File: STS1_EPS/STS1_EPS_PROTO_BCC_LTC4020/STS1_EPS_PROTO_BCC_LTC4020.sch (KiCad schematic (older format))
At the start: 13 parts, among them J1 1729267, J9 Output

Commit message: Reworked BCC
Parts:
- added C10, C9: 56µ, Capacitor_SMD:C_Elec_6.3x5.4, symbol Device:CP
- C1: value C -> 100n; footprint Capacitor_SMD:C_0805_2012Metric -> Capacitor_SMD:C_1812_4532Metric
- C2: value C -> 4µ7; footprint Capacitor_SMD:C_0805_2012Metric -> Capacitor_SMD:C_1812_4532Metric
- C3: value CP -> 56µ; footprint Capacitor_SMD:C_0805_2012Metric -> Capacitor_SMD:C_Elec_6.3x5.4
- renumbered J9 to J2
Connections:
- net EPS Battery Charger/Vout: now also C10.1, C9.1
- net GND: now also C10.2, C9.2
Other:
- moved on the sheet: C1, C2
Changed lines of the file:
@@
 L power:GND #PWR011
 U 1 1 60D46E13
-P 7700 1750
-F 0 "#PWR011" H 7700 1500 50  0001 C CNN
-F 1 "GND" H 7705 1577 50  0000 C CNN
-F 2 "" H 7700 1750 50  0001 C CNN
-F 3 "" H 7700 1750 50  0001 C CNN
-	1    7700 1750
+P 7700 1800
+F 0 "#PWR011" H 7700 1550 50  0001 C CNN
+F 1 "GND" H 7705 1627 50  0000 C CNN
+F 2 "" H 7700 1800 50  0001 C CNN
+F 3 "" H 7700 1800 50  0001 C CNN
+	1    7700 1800
 	1    0    0    -1
 $EndComp
@@
 L power:GND #PWR010
 U 1 1 60D46A71
-P 7350 1750
-F 0 "#PWR010" H 7350 1500 50  0001 C CNN
-F 1 "GND" H 7355 1577 50  0000 C CNN
-F 2 "" H 7350 1750 50  0001 C CNN
-F 3 "" H 7350 1750 50  0001 C CNN
-	1    7350 1750
+P 7300 1800
+F 0 "#PWR010" H 7300 1550 50  0001 C CNN
+F 1 "GND" H 7305 1627 50  0000 C CNN
+F 2 "" H 7300 1800 50  0001 C CNN
+F 3 "" H 7300 1800 50  0001 C CNN
+	1    7300 1800
 	1    0    0    -1
 $EndComp
@@
 L power:GND #PWR09
 U 1 1 60D462E6
-P 7000 1750
-F 0 "#PWR09" H 7000 1500 50  0001 C CNN
-F 1 "GND" H 7005 1577 50  0000 C CNN
-F 2 "" H 7000 1750 50  0001 C CNN
-F 3 "" H 7000 1750 50  0001 C CNN
-	1    7000 1750
+P 6850 1800
+F 0 "#PWR09" H 6850 1550 50  0001 C CNN
+F 1 "GND" H 6855 1627 50  0000 C CNN
+F 2 "" H 6850 1800 50  0001 C CNN
+F 3 "" H 6850 1800 50  0001 C CNN
+	1    6850 1800
 	1    0    0    -1
 $EndComp
@@
 P 7700 1600
 F 0 "C3" H 7818 1646 50  0000 L CNN
-F 1 "CP" H 7818 1555 50  0000 L CNN
-F 2 "Capacitor_SMD:C_0805_2012Metric" H 7738 1450 50  0001 C CNN
-F 3 "~" H 7700 1600 50  0001 C CNN
+F 1 "56µ" H 7818 1555 50  0000 L CNN
+F 2 "Capacitor_SMD:C_Elec_6.3x5.4" H 7738 1450 50  0001 C CNN
+F 3 "https://www.mouser.at/datasheet/2/293/e_gyc-1903391.pdf" H 7700 1600 50  0001 C CNN
 	1    7700 1600
 	1    0    0    -1
 $EndComp
-Wire Wire Line
-	7350 1450 7700 1450
 $Comp
 L Device:C C2
 U 1 1 60D44B49
-P 7350 1600
-F 0 "C2" H 7465 1646 50  0000 L CNN
-F 1 "C" H 7465 1555 50  0000 L CNN
-F 2 "Capacitor_SMD:C_0805_2012Metric" H 7388 1450 50  0001 C CNN
-F 3 "~" H 7350 1600 50  0001 C CNN
-	1    7350 1600
-	1    0    0    -1
-$EndComp
-Connection ~ 7350 1450
-Wire Wire Line
-	7000 1450 7350 1450
+P 7300 1600
+F 0 "C2" H 7415 1646 50  0000 L CNN
+F 1 "4µ7" H 7415 1555 50  0000 L CNN
+F 2 "Capacitor_SMD:C_1812_4532Metric" H 7338 1450 50  0001 C CNN
+F 3 "~" H 7300 1600 50  0001 C CNN
+	1    7300 1600
+	1    0    0    -1
+$EndComp
 $Comp
 L Device:C C1
 U 1 1 60D43AF5
-P 7000 1600
-F 0 "C1" H 7115 1646 50  0000 L CNN
-F 1 "C" H 7115 1555 50  0000 L CNN
-F 2 "Capacitor_SMD:C_0805_2012Metric" H 7038 1450 50  0001 C CNN
-F 3 "~" H 7000 1600 50  0001 C CNN
-	1    7000 1600
-	1    0    0    -1
-$EndComp
-Connection ~ 7000 1450
-Wire Wire Line
-	6000 1450 7000 1450
+P 6850 1600
+F 0 "C1" H 6965 1646 50  0000 L CNN
+F 1 "100n" H 6965 1555 50  0000 L CNN
+F 2 "Capacitor_SMD:C_1812_4532Metric" H 6888 1450 50  0001 C CNN
+F 3 "~" H 6850 1600 50  0001 C CNN
+	1    6850 1600
+	1    0    0    -1
+$EndComp
+Connection ~ 6850 1450
+Wire Wire Line
+	6000 1450 6850 1450
 $Sheet
 S 5300 1350 700  200
@@
 $EndSheet
 $Comp
-L 2021-06-25_11-05-00:1725656 J9
+L 2021-06-25_11-05-00:1725656 J2
 U 1 1 60D71756
 P 10050 1450
-F 0 "J9" H 10578 1453 60  0000 L CNN
+F 0 "J2" H 10578 1453 60  0000 L CNN
 F 1 "Output" H 10578 1347 60  0000 L CNN
 F 2 "footprints:1725656" H 10450 1390 60  0001 C CNN
@@
 $EndComp
 Wire Wire Line
-	10050 1450 7700 1450
+	10050 1450 8600 1450
 Connection ~ 7700 1450
 $Comp
@@
 $EndComp
 $Comp
-L power:GND #PWR0101
+L power:GND #PWR01
 U 1 1 60D850C0
 P 1500 1550
-F 0 "#PWR0101" H 1500 1300 50  0001 C CNN
+F 0 "#PWR01" H 1500 1300 50  0001 C CNN
 F 1 "GND" H 1505 1377 50  0000 C CNN
 F 2 "" H 1500 1550 50  0001 C CNN
@@
 $EndComp
 $Comp
-L power:GND #PWR0102
+L power:GND #PWR02
 U 1 1 60D860B9
 P 1500 1750
-F 0 "#PWR0102" H 1500 1500 50  0001 C CNN
+F 0 "#PWR02" H 1500 1500 50  0001 C CNN
 F 1 "GND" H 1505 1577 50  0000 C CNN
 F 2 "" H 1500 1750 50  0001 C CNN
@@
 $EndComp
 $Comp
-L power:GND #PWR0103
+L power:GND #PWR03
 U 1 1 60D865CE
 P 1500 1950
-F 0 "#PWR0103" H 1500 1700 50  0001 C CNN
+F 0 "#PWR03" H 1500 1700 50  0001 C CNN
 F 1 "GND" H 1505 1777 50  0000 C CNN
 F 2 "" H 1500 1950 50  0001 C CNN
@@
 $EndComp
 $Comp
-L power:GND #PWR0104
+L power:GND #PWR04
 U 1 1 60D8699D
 P 1500 2150
-F 0 "#PWR0104" H 1500 1900 50  0001 C CNN
+F 0 "#PWR04" H 1500 1900 50  0001 C CNN
 F 1 "GND" H 1505 1977 50  0000 C CNN
 F 2 "" H 1500 2150 50  0001 C CNN
@@
 $EndComp
 $Comp
-L power:GND #PWR0105
+L power:GND #PWR05
 U 1 1 60D86C57
 P 1500 2350
-F 0 "#PWR0105" H 1500 2100 50  0001 C CNN
+F 0 "#PWR05" H 1500 2100 50  0001 C CNN
 F 1 "GND" H 1505 2177 50  0000 C CNN
 F 2 "" H 1500 2350 50  0001 C CNN
@@
 $EndComp
 $Comp
-L power:GND #PWR0106
+L power:GND #PWR06
 U 1 1 60D86EA0
 P 1500 2550
-F 0 "#PWR0106" H 1500 2300 50  0001 C CNN
+F 0 "#PWR06" H 1500 2300 50  0001 C CNN
 F 1 "GND" H 1505 2377 50  0000 C CNN
 F 2 "" H 1500 2550 50  0001 C CNN
@@
 $EndComp
 $Comp
-L power:GND #PWR0107
+L power:GND #PWR07
 U 1 1 60D8714D
 P 1500 2750
-F 0 "#PWR0107" H 1500 2500 50  0001 C CNN
+F 0 "#PWR07" H 1500 2500 50  0001 C CNN
 F 1 "GND" H 1505 2577 50  0000 C CNN
 F 2 "" H 1500 2750 50  0001 C CNN
@@
 $EndComp
 $Comp
-L power:GND #PWR0108
+L power:GND #PWR08
 U 1 1 60D874BB
 P 1500 2950
-F 0 "#PWR0108" H 1500 2700 50  0001 C CNN
+F 0 "#PWR08" H 1500 2700 50  0001 C CNN
 F 1 "GND" H 1505 2777 50  0000 C CNN
 F 2 "" H 1500 2950 50  0001 C CNN
@@
 Wire Wire Line
 	2650 2650 2650 2850
+$Comp
+L Device:CP C9
+U 1 1 60DCCB93
+P 8150 1600
+F 0 "C9" H 8268 1646 50  0000 L CNN
+F 1 "56µ" H 8268 1555 50  0000 L CNN
+F 2 "Capacitor_SMD:C_Elec_6.3x5.4" H 8188 1450 50  0001 C CNN
+F 3 "https://www.mouser.at/datasheet/2/293/e_gyc-1903391.pdf" H 8150 1600 50  0001 C CNN
+	1    8150 1600
+	1    0    0    -1
+$EndComp
+$Comp
+L Device:CP C10
+U 1 1 60DCD030
+P 8600 1600
+F 0 "C10" H 8718 1646 50  0000 L CNN
+F 1 "56µ" H 8718 1555 50  0000 L CNN
+F 2 "Capacitor_SMD:C_Elec_6.3x5.4" H 8638 1450 50  0001 C CNN
+F 3 "https://www.mouser.at/datasheet/2/293/e_gyc-1903391.pdf" H 8600 1600 50  0001 C CNN
+	1    8600 1600
+	1    0    0    -1
+$EndComp
+Wire Wire Line
+	6850 1750 6850 1800
+Wire Wire Line
+	7300 1750 7300 1800
+Wire Wire Line
+	7700 1750 7700 1800
+$Comp
+L power:GND #PWR022
+U 1 1 60DCEDB8
+P 8150 1800
+F 0 "#PWR022" H 8150 1550 50  0001 C CNN
+F 1 "GND" H 8155 1627 50  0000 C CNN
+F 2 "" H 8150 1800 50  0001 C CNN
+F 3 "" H 8150 1800 50  0001 C CNN
+	1    8150 1800
+	1    0    0    -1
+$EndComp
+$Comp
+L power:GND #PWR023
+U 1 1 60DCF044
+P 8600 1800
+F 0 "#PWR023" H 8600 1550 50  0001 C CNN
+F 1 "GND" H 8605 1627 50  0000 C CNN
+F 2 "" H 8600 1800 50  0001 C CNN
+F 3 "" H 8600 1800 50  0001 C CNN
+	1    8600 1800
+	1    0    0    -1
+$EndComp
+Wire Wire Line
+	8150 1750 8150 1800
+Wire Wire Line
+	8600 1750 8600 1800
+Connection ~ 8150 1450
+Wire Wire Line
+	7700 1450 8150 1450
+Connection ~ 8600 1450
+Wire Wire Line
+	8150 1450 8600 1450
+Wire Wire Line
+	6850 1450 7300 1450
+Connection ~ 7300 1450
+Wire Wire Line
+	7300 1450 7700 1450
 $EndSCHEMATC

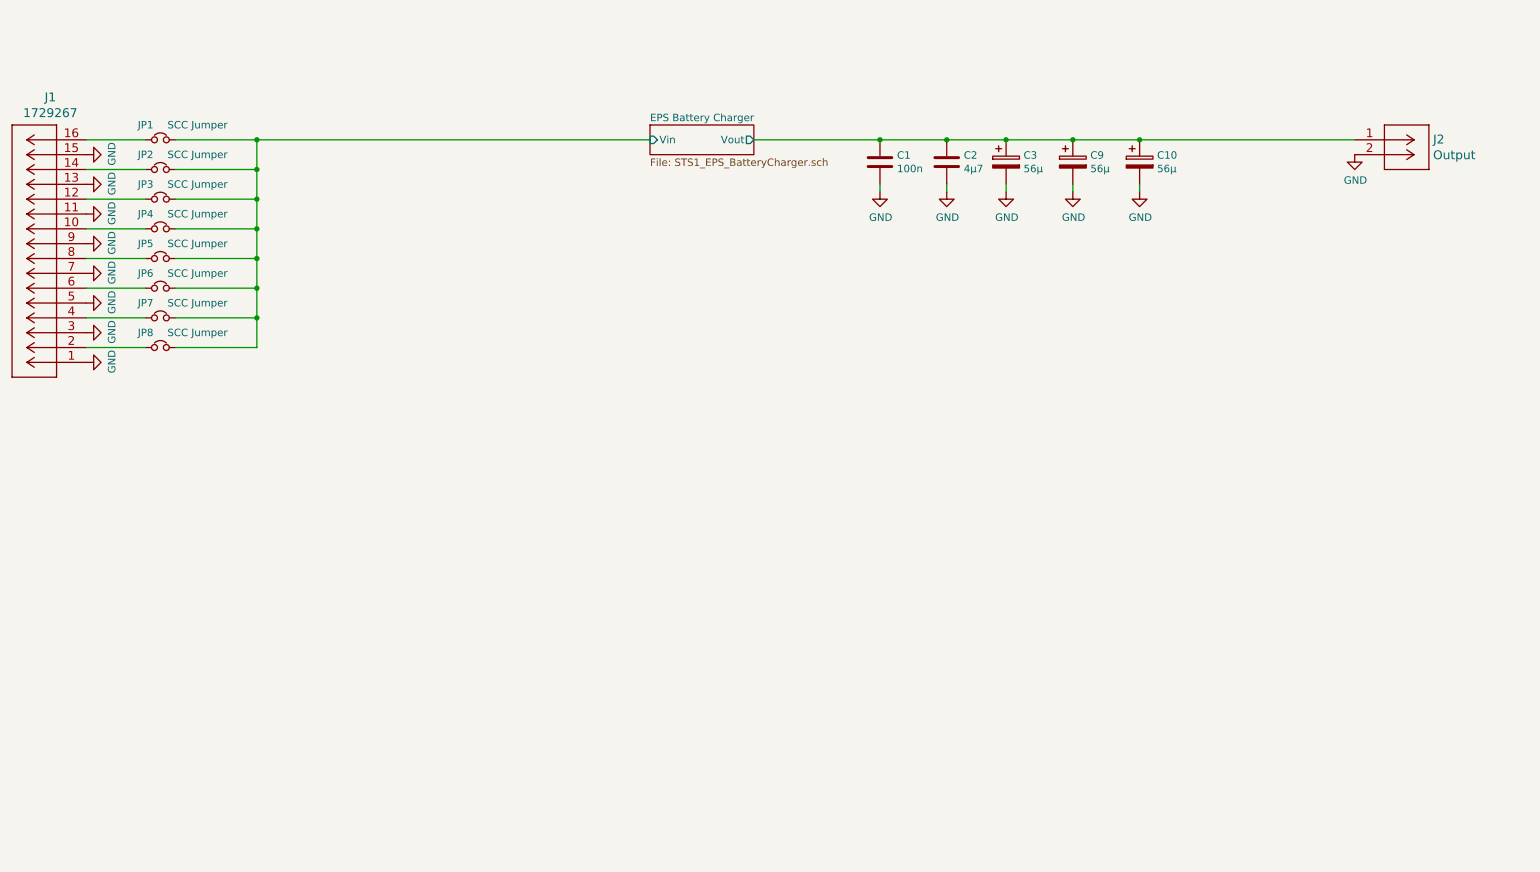
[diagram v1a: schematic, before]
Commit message: - STS1_EPS_PROTO_SCC_L6920 now uses the STS1 PCB template and is again ready for review. - WOrked on STS1_EPS_PROTO_BCC_LTC4020.
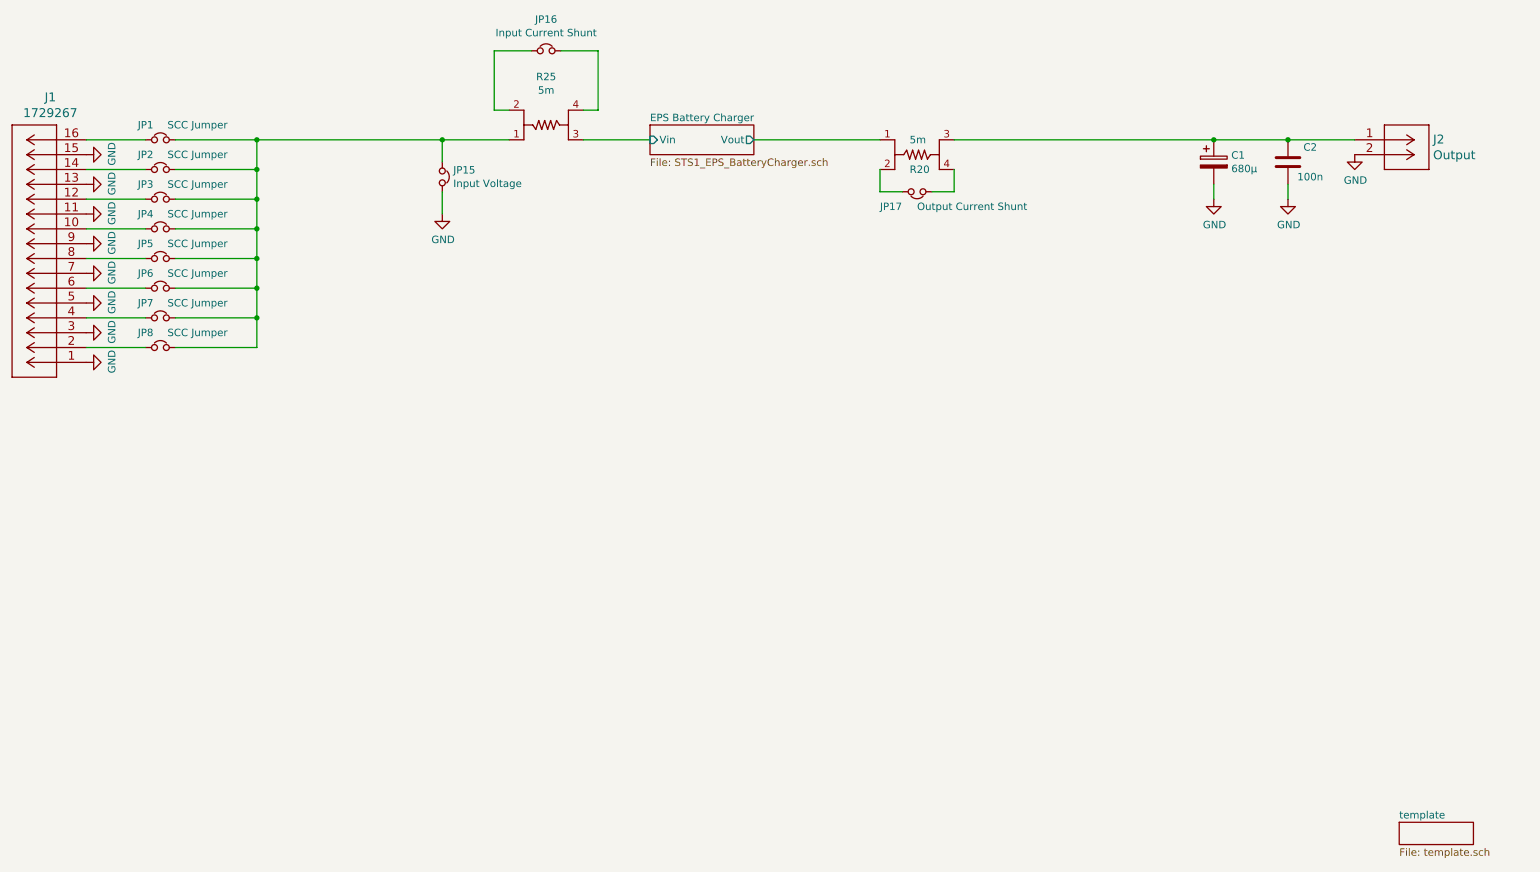
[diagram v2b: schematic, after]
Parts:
- removed C1: 100n, Capacitor_SMD:C_1812_4532Metric, symbol Device:C
- removed C10, C3, C9: 56µ, Capacitor_SMD:C_Elec_6.3x5.4, symbol Device:CP
- added C1: 680µ, Capacitor_Tantalum_SMD:CP_EIA-7361-438_AVX-U, symbol Device:CP
- added JP15: Input Voltage, Connector_PinHeader_2.54mm:PinHeader_1x02_P2.54mm_Vertical, symbol Device:Jumper_NC_Small
- added JP16: Input Current Shunt, Connector_PinHeader_2.54mm:PinHeader_1x02_P2.54mm_Vertical, symbol Device:Jumper_NC_Small
- added JP17: Output Current Shunt, Connector_PinHeader_2.54mm:PinHeader_1x02_P2.54mm_Vertical, symbol Device:Jumper_NC_Small
- added R20, R25: 5m, footprints:CST0612-FC-R002E, symbol 2021-06-29_19-28-22:CST0612-FC-R002E
- C2: value 4µ7 -> 100n; footprint Capacitor_SMD:C_1812_4532Metric -> Capacitor_SMD:C_0805_2012Metric
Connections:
- net EPS Battery Charger/Vin: now also R25.3; no longer JP1.2, JP2.2, JP3.2, JP4.2, JP5.2, JP6.2, JP7.2, JP8.2
- net EPS Battery Charger/Vout: now also R20.1; no longer C2.1, J2.1
- net GND: now also C2.1, C1.2, JP15.2; no longer C2.2
- new net: C1.1, C2.2, J2.1, R20.3
- new net: JP1.2, JP15.1, JP2.2, JP3.2, JP4.2, JP5.2, JP6.2, JP7.2, JP8.2, R25.1
- new net: JP16.1, R25.2
- new net: JP16.2, R25.4
- new net: JP17.2, R20.2
- new net: JP17.1, R20.4
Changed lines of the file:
@@
 $Descr A4 11693 8268
 encoding utf-8
-Sheet 1 2
+Sheet 1 4
 Title ""
 Date ""
@@
 Comment4 ""
 $EndDescr
-$Comp
-L power:GND #PWR011
-U 1 1 60D46E13
-P 7700 1800
-F 0 "#PWR011" H 7700 1550 50  0001 C CNN
-F 1 "GND" H 7705 1627 50  0000 C CNN
-F 2 "" H 7700 1800 50  0001 C CNN
-F 3 "" H 7700 1800 50  0001 C CNN
-	1    7700 1800
-	1    0    0    -1
-$EndComp
-$Comp
-L power:GND #PWR010
-U 1 1 60D46A71
-P 7300 1800
-F 0 "#PWR010" H 7300 1550 50  0001 C CNN
-F 1 "GND" H 7305 1627 50  0000 C CNN
-F 2 "" H 7300 1800 50  0001 C CNN
-F 3 "" H 7300 1800 50  0001 C CNN
-	1    7300 1800
-	1    0    0    -1
-$EndComp
-$Comp
-L power:GND #PWR09
-U 1 1 60D462E6
-P 6850 1800
-F 0 "#PWR09" H 6850 1550 50  0001 C CNN
-F 1 "GND" H 6855 1627 50  0000 C CNN
-F 2 "" H 6850 1800 50  0001 C CNN
-F 3 "" H 6850 1800 50  0001 C CNN
-	1    6850 1800
-	1    0    0    -1
-$EndComp
-$Comp
-L Device:CP C3
-U 1 1 60D4556F
-P 7700 1600
-F 0 "C3" H 7818 1646 50  0000 L CNN
-F 1 "56µ" H 7818 1555 50  0000 L CNN
-F 2 "Capacitor_SMD:C_Elec_6.3x5.4" H 7738 1450 50  0001 C CNN
-F 3 "https://www.mouser.at/datasheet/2/293/e_gyc-1903391.pdf" H 7700 1600 50  0001 C CNN
-	1    7700 1600
-	1    0    0    -1
-$EndComp
-$Comp
-L Device:C C2
-U 1 1 60D44B49
-P 7300 1600
-F 0 "C2" H 7415 1646 50  0000 L CNN
-F 1 "4µ7" H 7415 1555 50  0000 L CNN
-F 2 "Capacitor_SMD:C_1812_4532Metric" H 7338 1450 50  0001 C CNN
-F 3 "~" H 7300 1600 50  0001 C CNN
-	1    7300 1600
-	1    0    0    -1
-$EndComp
-$Comp
-L Device:C C1
-U 1 1 60D43AF5
-P 6850 1600
-F 0 "C1" H 6965 1646 50  0000 L CNN
-F 1 "100n" H 6965 1555 50  0000 L CNN
-F 2 "Capacitor_SMD:C_1812_4532Metric" H 6888 1450 50  0001 C CNN
-F 3 "~" H 6850 1600 50  0001 C CNN
-	1    6850 1600
-	1    0    0    -1
-$EndComp
-Connection ~ 6850 1450
-Wire Wire Line
-	6000 1450 6850 1450
 $Sheet
 S 5300 1350 700  200
@@
 	1    0    0    -1
 $EndComp
-Wire Wire Line
-	10050 1450 8600 1450
-Connection ~ 7700 1450
 $Comp
 L 2021-06-25_19-38-22:1729267 J1
@@
 $EndComp
 Wire Wire Line
-	5300 1450 2650 1450
-Wire Wire Line
 	2100 1650 2650 1650
 Connection ~ 2650 1450
@@
 Wire Wire Line
 	2650 2650 2650 2850
-$Comp
-L Device:CP C9
-U 1 1 60DCCB93
-P 8150 1600
-F 0 "C9" H 8268 1646 50  0000 L CNN
-F 1 "56µ" H 8268 1555 50  0000 L CNN
-F 2 "Capacitor_SMD:C_Elec_6.3x5.4" H 8188 1450 50  0001 C CNN
-F 3 "https://www.mouser.at/datasheet/2/293/e_gyc-1903391.pdf" H 8150 1600 50  0001 C CNN
-	1    8150 1600
-	1    0    0    -1
-$EndComp
-$Comp
-L Device:CP C10
-U 1 1 60DCD030
-P 8600 1600
-F 0 "C10" H 8718 1646 50  0000 L CNN
-F 1 "56µ" H 8718 1555 50  0000 L CNN
-F 2 "Capacitor_SMD:C_Elec_6.3x5.4" H 8638 1450 50  0001 C CNN
-F 3 "https://www.mouser.at/datasheet/2/293/e_gyc-1903391.pdf" H 8600 1600 50  0001 C CNN
-	1    8600 1600
-	1    0    0    -1
-$EndComp
-Wire Wire Line
-	6850 1750 6850 1800
-Wire Wire Line
-	7300 1750 7300 1800
-Wire Wire Line
-	7700 1750 7700 1800
-$Comp
-L power:GND #PWR022
-U 1 1 60DCEDB8
-P 8150 1800
-F 0 "#PWR022" H 8150 1550 50  0001 C CNN
-F 1 "GND" H 8155 1627 50  0000 C CNN
-F 2 "" H 8150 1800 50  0001 C CNN
-F 3 "" H 8150 1800 50  0001 C CNN
-	1    8150 1800
-	1    0    0    -1
-$EndComp
-$Comp
-L power:GND #PWR023
-U 1 1 60DCF044
-P 8600 1800
-F 0 "#PWR023" H 8600 1550 50  0001 C CNN
-F 1 "GND" H 8605 1627 50  0000 C CNN
-F 2 "" H 8600 1800 50  0001 C CNN
-F 3 "" H 8600 1800 50  0001 C CNN
-	1    8600 1800
-	1    0    0    -1
-$EndComp
-Wire Wire Line
-	8150 1750 8150 1800
-Wire Wire Line
-	8600 1750 8600 1800
-Connection ~ 8150 1450
-Wire Wire Line
-	7700 1450 8150 1450
-Connection ~ 8600 1450
-Wire Wire Line
-	8150 1450 8600 1450
-Wire Wire Line
-	6850 1450 7300 1450
-Connection ~ 7300 1450
-Wire Wire Line
-	7300 1450 7700 1450
+$Sheet
+S 10350 6050 500  150
+U 60E09456
+F0 "template" 50
+F1 "template.sch" 50
+$EndSheet
+$Comp
+L Device:Jumper_NC_Small JP15
+U 1 1 60E288CD
+P 3900 1700
+F 0 "JP15" V 3854 1774 50  0000 L CNN
+F 1 "Input Voltage" V 3945 1774 50  0000 L CNN
+F 2 "Connector_PinHeader_2.54mm:PinHeader_1x02_P2.54mm_Vertical" H 3900 1700 50  0001 C CNN
+F 3 "~" H 3900 1700 50  0001 C CNN
+	1    3900 1700
+	0    1    1    0
+$EndComp
+$Comp
+L power:GND #PWR0106
+U 1 1 60E29213
+P 3900 1950
+F 0 "#PWR0106" H 3900 1700 50  0001 C CNN
+F 1 "GND" H 3905 1777 50  0000 C CNN
+F 2 "" H 3900 1950 50  0001 C CNN
+F 3 "" H 3900 1950 50  0001 C CNN
+	1    3900 1950
+	1    0    0    -1
+$EndComp
+Wire Wire Line
+	3900 1600 3900 1450
+Wire Wire Line
+	3900 1450 2650 1450
+Wire Wire Line
+	3900 1800 3900 1950
+$Comp
+L 2021-06-29_19-28-22:CST0612-FC-R002E R25
+U 1 1 60E2A7E7
+P 3800 1400
+F 0 "R25" H 4600 1025 50  0000 C CNN
+F 1 "5m" H 4600 1116 50  0000 C CNN
+F 2 "footprints:CST0612-FC-R002E" H 3800 1400 50  0001 C CNN
+F 3 "~" H 3800 1400 50  0001 C CNN
+	1    3800 1400
+	1    0    0    1
+$EndComp
+Wire Wire Line
+	4350 1450 3900 1450
+Connection ~ 3900 1450
+Wire Wire Line
+	4850 1450 5300 1450
+$Comp
+L Device:Jumper_NC_Small JP16
+U 1 1 60E33399
+P 4600 850
+F 0 "JP16" H 4600 1062 50  0000 C CNN
+F 1 "Input Current Shunt" H 4600 971 50  0000 C CNN
+F 2 "Connector_PinHeader_2.54mm:PinHeader_1x02_P2.54mm_Vertical" H 4600 850 50  0001 C CNN
+F 3 "~" H 4600 850 50  0001 C CNN
+	1    4600 850
+	1    0    0    -1
+$EndComp
+Wire Wire Line
+	4500 850  4250 850
+Wire Wire Line
+	4250 850  4250 1250
+Wire Wire Line
+	4250 1250 4350 1250
+Wire Wire Line
+	4700 850  4950 850
+Wire Wire Line
+	4950 850  4950 1250
+Wire Wire Line
+	4950 1250 4850 1250
+$Comp
+L 2021-06-29_19-28-22:CST0612-FC-R002E R20
+U 1 1 6108DE0B
+P 6300 1500
+AR Path="/6108DE0B" Ref="R20"  Part="1"
+AR Path="/60B53241/6108DE0B" Ref="R?"  Part="1"
+F 0 "R20" H 7050 1350 50  0000 L CNN
+F 1 "5m" H 7050 1550 50  0000 L CNN
+F 2 "footprints:CST0612-FC-R002E" V 6230 1500 50  0001 C CNN
+F 3 "https://www.mouser.at/datasheet/2/54/cst0612-777607.pdf" H 6300 1500 50  0001 C CNN
+	1    6300 1500
+	1    0    0    -1
+$EndComp
+$Comp
+L Device:Jumper_NC_Small JP?
+U 1 1 6108DE12
+P 7100 1800
+AR Path="/60B53241/6108DE12" Ref="JP?"  Part="1"
+AR Path="/6108DE12" Ref="JP17"  Part="1"
+F 0 "JP17" H 7350 1900 50  0000 R CNN
+F 1 "Output Current Shunt" H 7100 1900 50  0000 R CNN
+F 2 "Connector_PinHeader_2.54mm:PinHeader_1x02_P2.54mm_Vertical" H 7100 1800 50  0001 C CNN
+F 3 "~" H 7100 1800 50  0001 C CNN
+	1    7100 1800
+	-1   0    0    1
+$EndComp
+Wire Wire Line
+	7200 1800 7350 1800
+Wire Wire Line
+	7350 1800 7350 1650
+Wire Wire Line
+	7000 1800 6850 1800
+Wire Wire Line
+	6850 1800 6850 1650
+$Comp
+L Device:C C?
+U 1 1 611C3E0F
+P 9600 1600
+AR Path="/60B53241/611C3E0F" Ref="C?"  Part="1"
+AR Path="/611C3E0F" Ref="C2"  Part="1"
+F 0 "C2" H 9450 1500 50  0000 C CNN
+F 1 "100n" H 9450 1700 50  0000 C CNN
+F 2 "Capacitor_SMD:C_0805_2012Metric" H 9638 1450 50  0001 C CNN
+F 3 "~" H 9600 1600 50  0001 C CNN
+	1    9600 1600
+	-1   0    0    1
+$EndComp
+$Comp
+L power:GND #PWR?
+U 1 1 611C3E15
+P 9600 1850
+AR Path="/60B53241/611C3E15" Ref="#PWR?"  Part="1"
+AR Path="/611C3E15" Ref="#PWR0107"  Part="1"
+F 0 "#PWR0107" H 9600 1600 50  0001 C CNN
+F 1 "GND" H 9605 1677 50  0000 C CNN
+F 2 "" H 9600 1850 50  0001 C CNN
+F 3 "" H 9600 1850 50  0001 C CNN
+	1    9600 1850
+	1    0    0    -1
+$EndComp
+Wire Wire Line
+	9600 1750 9600 1850
+$Comp
+L Device:CP C?
+U 1 1 611C3E1C
+P 9100 1600
+AR Path="/60B53241/611C3E1C" Ref="C?"  Part="1"
+AR Path="/611C3E1C" Ref="C1"  Part="1"
+F 0 "C1" H 9218 1646 50  0000 L CNN
+F 1 "680µ" H 9218 1555 50  0000 L CNN
+F 2 "Capacitor_Tantalum_SMD:CP_EIA-7361-438_AVX-U" H 9138 1450 50  0001 C CNN
+F 3 "https://www.mouser.at/datasheet/2/40/catalogue_TRM-1021477.pdf" H 9100 1600 50  0001 C CNN
+	1    9100 1600
+	1    0    0    -1
+$EndComp
+$Comp
+L power:GND #PWR?
+U 1 1 611C3E22
+P 9100 1850
+AR Path="/60B53241/611C3E22" Ref="#PWR?"  Part="1"
+AR Path="/611C3E22" Ref="#PWR0108"  Part="1"
+F 0 "#PWR0108" H 9100 1600 50  0001 C CNN
+F 1 "GND" H 9105 1677 50  0000 C CNN
+F 2 "" H 9100 1850 50  0001 C CNN
+F 3 "" H 9100 1850 50  0001 C CNN
+	1    9100 1850
+	1    0    0    -1
+$EndComp
+Wire Wire Line
+	9100 1750 9100 1850
+Wire Wire Line
+	6000 1450 6850 1450
+Wire Wire Line
+	7350 1450 9100 1450
+Connection ~ 9100 1450
+Wire Wire Line
+	9100 1450 9600 1450
+Connection ~ 9600 1450
+Wire Wire Line
+	9600 1450 10050 1450
 $EndSCHEMATC
